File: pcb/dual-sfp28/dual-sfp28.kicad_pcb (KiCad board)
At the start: 4 copper layers, 89 x 19.5 mm, 50 parts, among them J1 CONN_01X10, J2 ARF6-08-S-D-A-K-TR, J3 CONN_SFP_HOST_DUAL, J4 SCREWHOLE, M1 LOGO, M2 LOGO, M3 LOGO, U1 TCA6424A

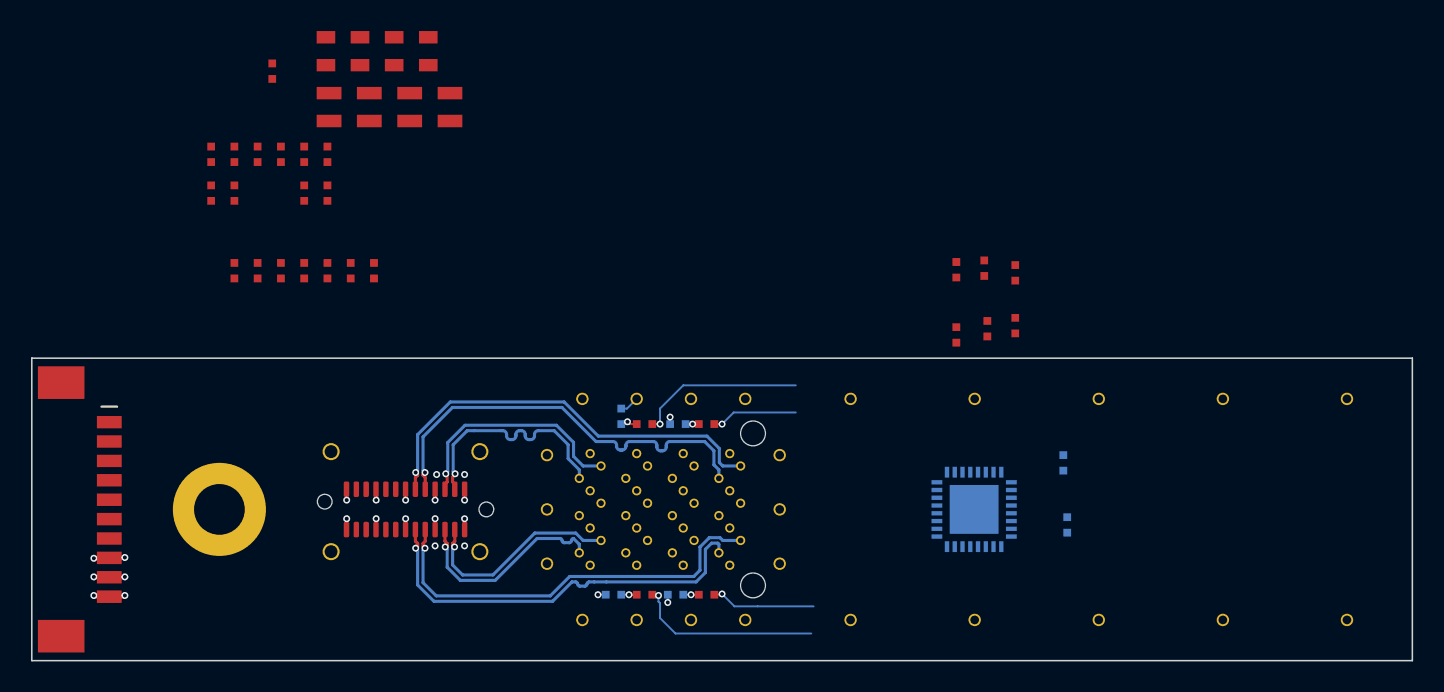
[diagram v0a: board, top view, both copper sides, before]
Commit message: Initial versino of dual-sfp28 is fully routed and ready for review
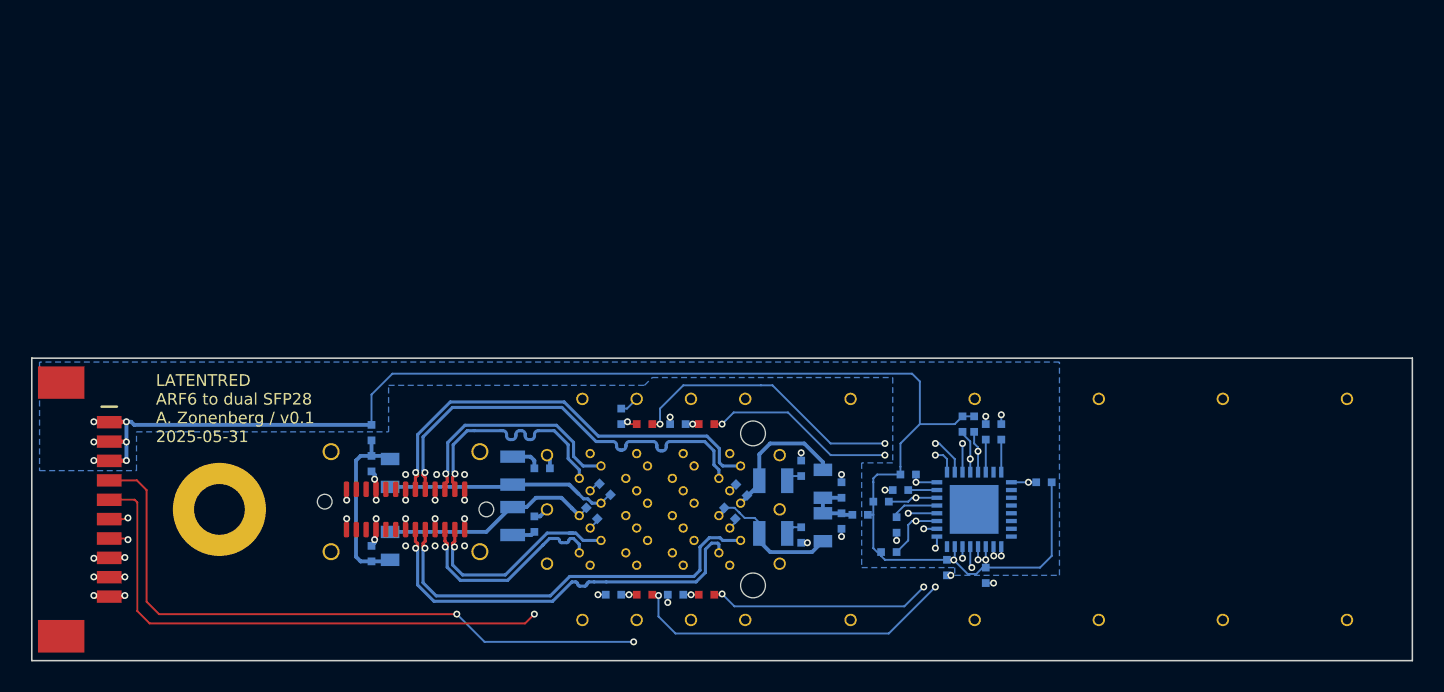
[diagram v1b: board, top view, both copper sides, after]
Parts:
- C10, C11, C12, C13, C14, C3, C4, C5, C6, C7, C8, C9, L1, L2, L3, L4, R10, R11, R12, R13, R14, R15, R16, R17, R18, R19, R20, R5, R6, R7, R8, R9: moved to B.Cu
- moved R6 53.2 mm to (93.5, 70.2), turned to -90 degrees
- moved R7 50.8 mm to (92.5, 70.2), turned to -90 degrees
- moved R15 47.9 mm to (84.4, 75.6), turned to 0 degrees
- moved L1 44.4 mm to (82.0, 76.4)
- moved R16 44.0 mm to (80.6, 76.9)
- moved R10 42.9 mm to (87.0, 74.0), turned to 0 degrees
- moved R11 42.5 mm to (86.8, 76.2)
- moved C3 42.3 mm to (83.2, 76.0), turned to -90 degrees
- moved L2 40.8 mm to (82.0, 73.6), turned to -90 degrees
- moved R17 40.5 mm to (80.6, 72.6), turned to -90 degrees
- moved C4 40.2 mm to (83.2, 74.0)
- moved C5 39.7 mm to (78.8, 76.8), turned to 0 degrees
- moved C6 35.5 mm to (78.8, 73.4), turned to 0 degrees
- moved C14 35.2 mm to (67.1, 75.5), turned to -45 degrees
- moved C7 32.9 mm to (76.0, 75.5), turned to -45 degrees
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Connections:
- R10 pad 2: Net-(U1-P22) -> Net-(U1-P06)
- R11 pad 2: Net-(U1-P23) -> Net-(U1-P04)
- R6 pad 2: Net-(U1-P12) -> Net-(U1-P17)
- R7 pad 2: Net-(U1-P13) -> Net-(U1-P15)
- U1 pad 10: /SFP0_TX_DISABLE -> /LED2_P
- U1 pad 11: Net-(U1-P12) -> /SFP1_TX_DISABLE
- U1 pad 12: Net-(U1-P13) -> /SFP1_TX_FAULT
- U1 pad 14: /SFP0_RX_LOS -> Net-(U1-P15)
- U1 pad 16: unconnected-(U1-P17-Pad16) -> Net-(U1-P17)
- U1 pad 17: /SFP1_TX_FAULT -> /SFP0_RX_LOS
- U1 pad 18: /SFP1_TX_DISABLE -> unconnected-(U1-P21-Pad18)
- U1 pad 19: Net-(U1-P22) -> unconnected-(U1-P22-Pad19)
- U1 pad 20: Net-(U1-P23) -> unconnected-(U1-P23-Pad20)
- U1 pad 21: /SFP1_MOD_ABS -> unconnected-(U1-P24-Pad21)
- U1 pad 22: /SFP1_RX_LOS -> unconnected-(U1-P25-Pad22)
- U1 pad 3: /LED2_P -> /SFP0_TX_FAULT
- U1 pad 4: /LED3_P -> /SFP0_TX_DISABLE
- U1 pad 5: unconnected-(U1-P04-Pad5) -> Net-(U1-P04)
- U1 pad 6: unconnected-(U1-P05-Pad6) -> /SFP1_RX_LOS
- U1 pad 7: unconnected-(U1-P06-Pad7) -> Net-(U1-P06)
- U1 pad 8: unconnected-(U1-P07-Pad8) -> /SFP1_MOD_ABS
- U1 pad 9: /SFP0_TX_FAULT -> /LED3_P
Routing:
- net /3V3: track 0.00 -> 106.5 mm, vias 0 -> 9
- net /I2C0_SDA: track 20.4 -> 75.7 mm, vias 0 -> 3
- net /I2C0_SCL: track 21.7 -> 75.5 mm, vias 0 -> 2
- net /I2C1_SCL: track 9.54 -> 42.0 mm, vias 0 -> 1
- net /I2C1_SDA: track 9.76 -> 41.8 mm, vias 0 -> 1
- net /GND: track 240.5 -> 267.9 mm, vias 23 -> 35
- net /SFP0_RX_LOS: track 16.8 -> 37.7 mm, vias 0 -> 1
- net /SFP0_TX_FAULT: track 17.1 -> 33.8 mm, vias 0 -> 1
- net /SFP0_VDD_RX: track 0.00 -> 15.1 mm
- net /SFP0_MOD_ABS: track 15.3 -> 29.9 mm, vias 0 -> 1
- net /SFP0_VDD_TX: track 0.00 -> 14.3 mm
- net /SFP0_RS0: track 16.8 -> 30.7 mm, vias 0 -> 1
- net /SFP0_TX_DISABLE: track 15.6 -> 29.2 mm, vias 0 -> 1
- net /SFP1_TX_FAULT: track 9.89 -> 23.3 mm, vias 0 -> 1
- net /LED2_P: track 10.9 -> 23.9 mm, vias 1 -> 3
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- added copper zone on B.Cu, net /3V3
- added copper zone on In1.Cu, net /GND
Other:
- board text added: "LATENTRED ARF6 to dual SFP28 A. Zonenberg / v0.1 2025-05-31"

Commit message: Updated dual-sfp28 board with final config for fab
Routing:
- net /SFP1_VDD_RX: track 9.99 -> 7.83 mm
- net /GND: track 267.9 -> 266.6 mm
- net /SFP1_MOD_ABS: track 19.8 -> 18.8 mm
- net /SFP1_TX_DISABLE: track 22.8 -> 22.1 mm
- net /SFP1_VDD_TX: track 11.1 -> 10.5 mm
- net /SFP0_VDD_RX: track 15.1 -> 14.5 mm
- net /3V3: track 106.5 -> 106.9 mm, vias 9 -> 6
